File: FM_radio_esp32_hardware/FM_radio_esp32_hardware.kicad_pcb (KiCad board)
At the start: 2 copper layers, 85 x 57 mm, 29 parts, among them J1 AudioJack2_Ground_SwitchT, J2 Conn_01x06, J4 Conn_02x03_Odd_Even, J5 Conn_01x02, SW1 SW_Push, SW2 SW_SPDT, U1 ESP32-WROOM-32D, U2 RDA5807

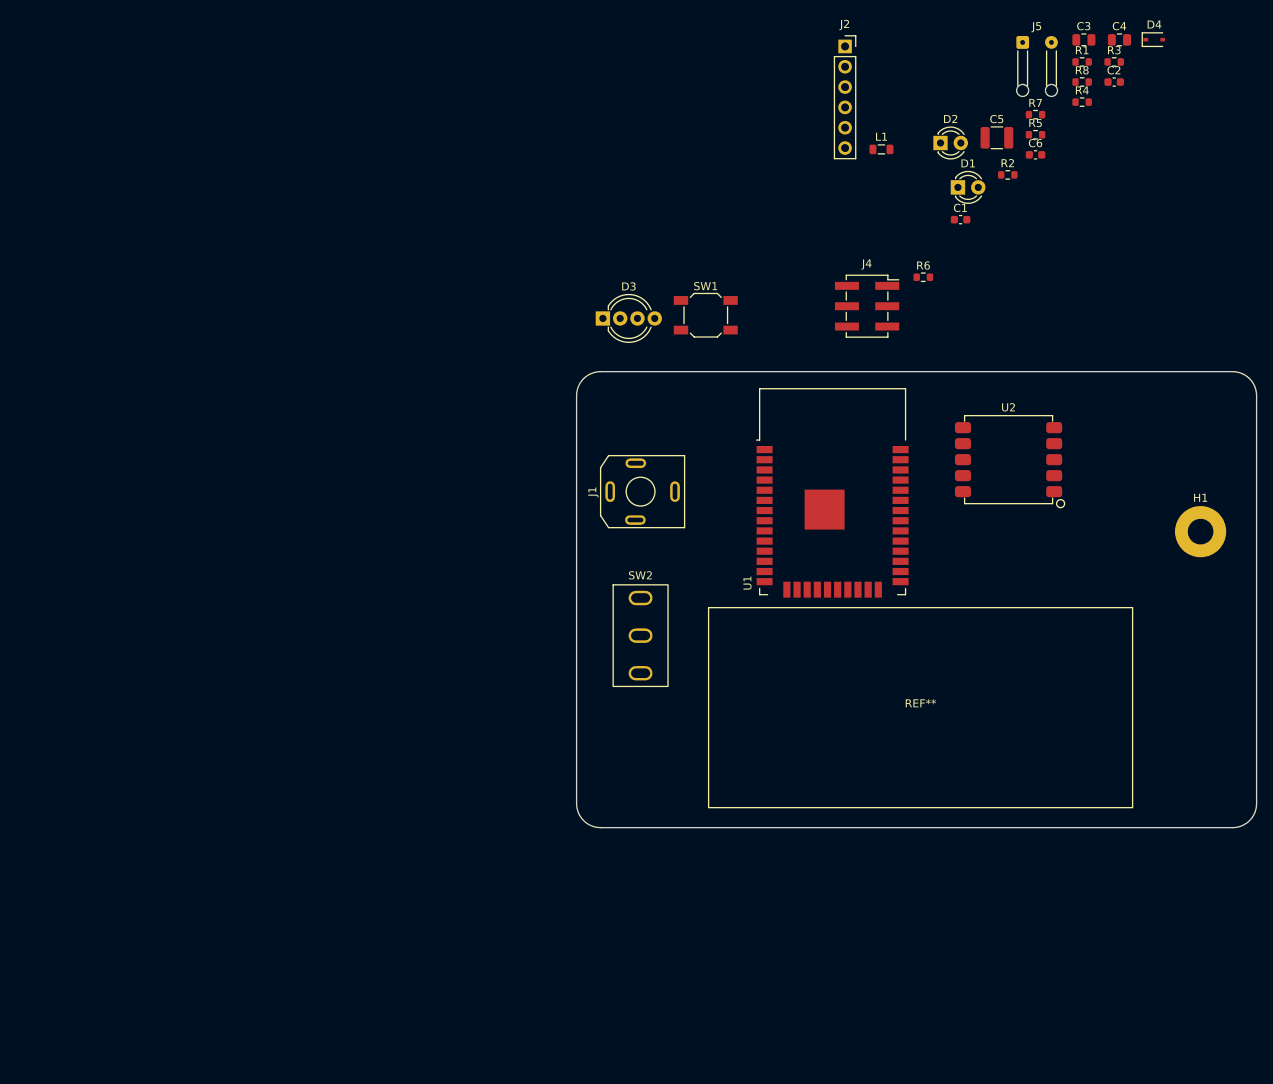
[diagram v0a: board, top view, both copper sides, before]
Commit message: added, side panel project. dimensions are need to be fixed
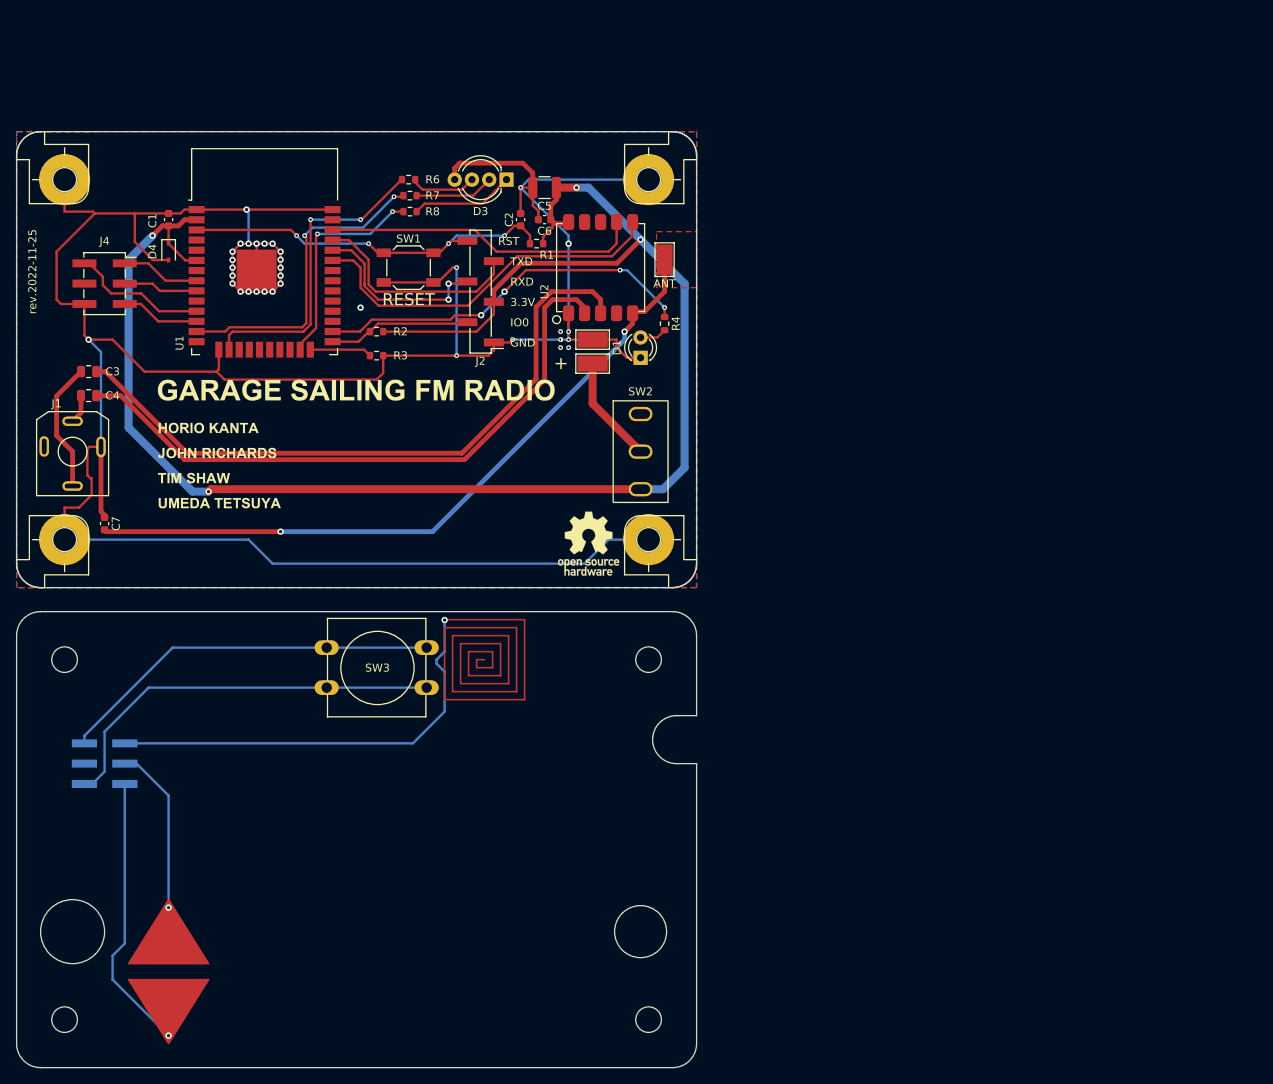
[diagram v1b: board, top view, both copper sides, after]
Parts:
- removed D2: LED, LED_THT:LED_D3.0mm
- removed J5: Conn_01x02, Connector_Wire:SolderWire-0.1sqmm_1x02_P3.6mm_D0.4mm_OD1mm_Relief
- removed L1: 1uH, Inductor_SMD:L_0805_2012Metric
- removed R5: 1k, Resistor_SMD:R_0603_1608Metric
- removed the REF** at (153.0, 105.0)
- added C7: 1nF, Capacitor_SMD:C_0603_1608Metric, F.Cu at (51.0, 82.0)
- added G***: LOGO, FM_radio_esp32:GS_text_logo_credit, F.Cu at (82.5, 72.0)
- added G***: LOGO, FM_radio_esp32:umeda_ninja, B.Cu at (86.0, 131.0)
- added G***: LOGO, FM_radio_esp32:electronics_fig_5, B.Cu at (110.0, 56.0)
- added H10: MountingHole, FM_radio_esp32:Hole_8mm, F.Cu at (47.0, 133.0)
- added H11: MountingHole, MountingHole:MountingHole_6.5mm, F.Cu at (118.0, 133.0)
- added H2: MountingHole_Pad, MountingHole:MountingHole_3.2mm_M3_Pad, F.Cu at (46.0, 39.0)
- added H3: MountingHole_Pad, MountingHole:MountingHole_3.2mm_M3_Pad, F.Cu at (46.0, 84.0)
- added H4: MountingHole_Pad, MountingHole:MountingHole_3.2mm_M3_Pad, F.Cu at (119.0, 84.0)
- added H5: MountingHole_Pad, MountingHole:MountingHole_3.2mm_M3_Pad, F.Cu at (119.0, 39.0)
- added H6: MountingHole, MountingHole:MountingHole_3.2mm_M3, F.Cu at (46.0, 99.0)
- added H7: MountingHole, MountingHole:MountingHole_3.2mm_M3, F.Cu at (46.0, 144.0)
- added H8: MountingHole, MountingHole:MountingHole_3.2mm_M3, F.Cu at (119.0, 144.0)
- added H9: MountingHole, MountingHole:MountingHole_3.2mm_M3, F.Cu at (119.0, 99.0)
- added J3: Conn_02x03_Odd_Even, Connector_PinHeader_2.54mm:PinHeader_2x03_P2.54mm_Vertical_SMD, B.Cu at (51.0, 112.0)
- added REF**: OSHW-Logo_7.5x8mm_SilkScreen, Symbol:OSHW-Logo_7.5x8mm_SilkScreen, F.Cu at (111.5, 84.5)
- added REF**: Case_Corner, FM_radio_esp32:Case_Corner, F.Cu at (125.0, 90.0)
- added REF**: Case_Corner, FM_radio_esp32:Case_Corner, F.Cu at (40.0, 90.0)
- added REF**: Case_Corner, FM_radio_esp32:Case_Corner, F.Cu at (40.0, 33.0)
- added REF**: Case_Corner, FM_radio_esp32:Case_Corner, F.Cu at (125.0, 33.0)
- added SW3: SW_SPST, Button_Switch_THT:SW_PUSH-12mm, F.Cu at (78.8, 97.5)
- added TP1: TestPoint, TestPoint:TestPoint_Keystone_5019_Minature, F.Cu at (112.0, 62.0)
- added TP2: TestPoint, TestPoint:TestPoint_Keystone_5019_Minature, F.Cu at (112.0, 59.0)
- D1: footprint LED_THT:LED_D3.0mm -> FM_radio_esp32:LED_D3.0mm
- H1: footprint MountingHole:MountingHole_3.2mm_M3_Pad -> TestPoint:TestPoint_Keystone_5019_Minature
- J2: footprint Connector_PinSocket_2.54mm:PinSocket_1x06_P2.54mm_Vertical -> Connector_PinHeader_2.54mm:PinHeader_1x06_P2.54mm_Vertical_SMD_Pin1Left
- moved C4 136.3 mm to (49.0, 66.0), turned to 180 degrees
- moved C3 131.1 mm to (49.0, 63.0), turned to 180 degrees
- moved D4 126.0 mm to (59.0, 48.0), turned to -90 degrees
- moved R3 99.2 mm to (85.0, 61.0)
- moved C1 99.0 mm to (59.0, 44.0), turned to -90 degrees
- moved J4 95.4 mm to (51.0, 52.0)
- moved R8 85.6 mm to (89.2, 43.0)
- moved R2 81.3 mm to (85.0, 58.0), turned to 180 degrees
- moved R7 78.8 mm to (89.2, 41.0)
- moved U1 77.1 mm to (71.0, 51.0)
- moved C2 76.2 mm to (103.0, 44.0), turned to 90 degrees
- moved H1 75.1 mm to (121.0, 49.0), turned to -90 degrees
- moved R1 71.9 mm to (105.0, 47.0), turned to 180 degrees
- moved J1 71.2 mm to (47.0, 73.0), turned to 0 degrees
- moved R6 65.5 mm to (89.0, 39.0)
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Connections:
- net Net-(L1-Pad2) renamed /ANT
- U1 pad 12: /TOUCH_1 -> /TOUCH_3
- U1 pad 8: /TOUCH_2 -> /TOUCH_1
- U1 pad 9: /TOUCH_3 -> /TOUCH_2
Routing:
- net GND: track 0.00 -> 375.9 mm, vias 0 -> 34
- net +3V3: track 0.00 -> 205.7 mm, vias 0 -> 4
- net /ANT: track 0.00 -> 88.1 mm, vias 0 -> 2
- net Net-(C3-Pad1): track 0.00 -> 82.8 mm
- net Net-(C4-Pad1): track 0.00 -> 78.8 mm
- net /T1: track 0.00 -> 53.9 mm, vias 0 -> 1
- net Net-(J3-Pad6): track 0.00 -> 50.7 mm
- net /RESET: track 0.00 -> 48.8 mm, vias 0 -> 4
- net Net-(J3-Pad2): track 0.00 -> 48.3 mm
- net /LED_1: track 0.00 -> 47.8 mm, vias 0 -> 4
- net /I2C_SDA: track 0.00 -> 46.4 mm
- net /T3: track 0.00 -> 40.4 mm, vias 0 -> 1
- net /LED_3_G: track 0.00 -> 39.6 mm, vias 0 -> 2
- net /I2C_SCL: track 0.00 -> 39.5 mm
- net /LED_3_B: track 0.00 -> 39.2 mm, vias 0 -> 2
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- added copper zone on F.Cu, net /ANT
- added copper zone on B.Cu, net GND
- added copper zone on F.Cu, net GND
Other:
- board size 85 x 57 mm -> 85 x 117 mm
- board text added: "+"
- board text added: "-"
- board text added: "3.3V"
- board text added: "ANT"
- board text added: "GND"
- board text added: "IO0"
- board text added: "RESET"
- board text added: "RST"
- board text added: "RXD"
- board text added: "TXD"
- board text added: "rev.2022-11-25"
